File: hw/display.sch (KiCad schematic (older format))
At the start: 1 part

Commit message: revision 2 pcb ordered from itead
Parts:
- removed U?: LPC1785FBD208_551QFP50, usevolt:usevolt-QFP208, symbol LPC1785FBD208_551QFP50
- added BT1: BATTERY_HOLDER_CH7410-2032LFSMD, usevolt:usevolt-BATTERY_HOLDER_CH7410-2032LF, symbol BATTERY_HOLDER_CH7410-2032LFSMD
- added C1, C2, C3, C32, C4, C5, C6, C7, C8: 100nF, kemet:Kemet-CAPC1608X85N, symbol 100nF
- added C22, C29: 12pF, kemet:Kemet-CAPC1608X85N, symbol 12pF
- added J1: AMPSEAL_14_POS_776261-1_V, usevolt:usevolt-AMPSEAL_14_POS_776261-1, symbol AMPSEAL_14_POS_776261-1_V
- added J4: HEADER_MOLEX_52207-0433, usevolt:HEADER_MOLEX_52207-0433, symbol HEADER_MOLEX_52207-0433
- added J5: HEADER_MOLEX_54104-4031, usevolt:HEADER_MOLEX_54104-4031, symbol HEADER_MOLEX_54104-4031
- added R1: 10K, multicomp:Multicomp-RESC1608X60N, symbol 10K
- added U1: MCP2551_SOIC8, usevolt:usevolt-SOIC8, symbol MCP2551_SOIC8
- added U2: ALLIANCE_AS4C4M16SA_TSOP_II, usevolt:usevolt-TSOP_II_54_PIN, symbol ALLIANCE_AS4C4M16SA_TSOP_II
- added U3: WINDBOND_W25Q32FV_SOIC8_W, usevolt:usevolt-SOIC8_W, symbol WINDBOND_W25Q32FV_SOIC8_W
- added U5, U6: MOSFET-N_2N7002W, usevolt:usevolt-SOT323, symbol MOSFET-N_2N7002W
- added X2: XTAL_ABS25-32.768KHZ-T, usevolt:usevolt-XTAL_32.768KHZ-T, symbol XTAL_ABS25-32.768KHZ-T
- added X3: BUZZER_PKM13EPYH4002-B0, usevolt:BUZZER_PKM13EPYH4002-B0, symbol BUZZER_PKM13EPYH4002-B0
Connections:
- net labels added: +3V3, +5V, A0, A1, A10, A11, A2, A3, A4, A5, A6, A7, A8, A9, BA0, BA1, BACKLIGHT, BCKL+, BCKL-, CANH, CANL, DCLK, DE, DQ0, DQ1, DQ10, DQ11, DQ12, DQ13, DQ14, DQ15, DQ2, DQ3, DQ4, DQ5, DQ6, DQ7, DQ8, DQ9, GND, HSYNC, PWR, VD0, VD1, VD10, VD11, VD12, VD13, VD14, VD15, VD16, VD17, VD18, VD19, VD2, VD20, VD21, VD22, VD23, VD3, VD4, VD5, VD6, VD7, VD8, VD9, VDD, VSYNC
- wire segments 0 -> 282
- no-connect marks 0 -> 11

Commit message: PCB was too big for itead, reduced size and ordered one
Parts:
- U1: footprint usevolt:usevolt-SOIC8 -> usevolt:SOIC8
- U2: footprint usevolt:usevolt-TSOP_II_54_PIN -> usevolt:TSOP_II_54_PIN
- U3: footprint usevolt:usevolt-SOIC8_W -> usevolt:SOIC8_W
- U5, U6: footprint usevolt:usevolt-SOT323 -> usevolt:SOT323
- X2: footprint usevolt:usevolt-XTAL_32.768KHZ-T -> usevolt:XTAL_32.768KHZ-T
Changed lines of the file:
@@
 F 0 "U1" H 3250 2846 45  0000 C CNN
 F 1 "MCP2551_SOIC8" H 3250 2930 45  0000 C CNN
-F 2 "usevolt:usevolt-SOIC8" H 2930 3450 20  0001 C CNN
+F 2 "usevolt:SOIC8" H 2930 3450 20  0001 C CNN
 F 3 "http://www.microchip.com/mymicrochip/filehandler.aspx?ddocname=en011797" H 2900 3520 60  0001 C CNN
 F 4 "9758569" H 3500 4120 60  0001 C CNN "2nd Source Part Number"
@@
 F 0 "U3" H 11300 3654 45  0000 C CNN
 F 1 "WINDBOND_W25Q32FV_SOIC8_W" H 11300 3570 45  0000 C CNN
-F 2 "usevolt:usevolt-SOIC8_W" H 11230 3450 20  0001 C CNN
+F 2 "usevolt:SOIC8_W" H 11230 3450 20  0001 C CNN
 F 3 "http://www.winbond.com/resource-files/w25q32fv%20revi%2010202015.pdf" H 10800 3520 60  0001 C CNN
 F 4 "Digi-Key" H 11100 3820 60  0001 C CNN "1st Source"
@@
 F 0 "U2" H 5300 5454 45  0000 C CNN
 F 1 "ALLIANCE_AS4C4M16SA_TSOP_II" H 5300 5370 45  0000 C CNN
-F 2 "usevolt:usevolt-TSOP_II_54_PIN" H 5430 4250 20  0001 C CNN
+F 2 "usevolt:TSOP_II_54_PIN" H 5430 4250 20  0001 C CNN
 F 3 "http://www.alliancememory.com/pdf/dram/64M-AS4C4M16SA-Automotive_v3.0_March%202015.pdf" H 4710 5330 60  0001 C CNN
 F 4 "1450-1258-ND" H 5110 5730 60  0001 C CNN "1st Source Part Number"
@@
 $Bitmap
 Pos 15800 10400
-Scale 1,000000
+Scale 1.000000
 Data
 89 50 4E 47 0D 0A 1A 0A 00 00 00 0D 49 48 44 52 00 00 00 7B 00 00 00 49 08 02 00 00 00 92 17 CE
@@
 F 0 "X2" V 7208 7698 45  0000 L CNN
 F 1 "XTAL_ABS25-32.768KHZ-T" V 7292 7698 45  0000 L CNN
-F 2 "usevolt:usevolt-XTAL_32.768KHZ-T" H 7330 7750 20  0001 C CNN
+F 2 "usevolt:XTAL_32.768KHZ-T" H 7330 7750 20  0001 C CNN
 F 3 "http://www.abracon.com/Resonators/abs25.pdf" H 7320 7620 60  0001 C CNN
 F 4 "1611824" H 7920 8220 60  0001 C CNN "2nd Source Part Number"
@@
 F 0 "U5" H 10400 7844 60  0000 C CNN
 F 1 "MOSFET-N_2N7002W" H 10400 7738 60  0000 C CNN
-F 2 "usevolt:usevolt-SOT323" H 10700 8900 60  0001 C CNN
+F 2 "usevolt:SOT323" H 10700 8900 60  0001 C CNN
 F 3 "http://www.onsemi.com/pub_link/Collateral/2N7002W-D.PDF" H 10550 9000 60  0001 C CNN
 F 4 "2533171" H 10975 8825 60  0001 C CNN "2nd Source Part Number"
@@
 F 0 "U6" H 13200 3350 60  0000 C CNN
 F 1 "MOSFET-N_2N7002W" H 13350 3450 60  0000 C CNN
-F 2 "usevolt:usevolt-SOT323" H 13500 4450 60  0001 C CNN
+F 2 "usevolt:SOT323" H 13500 4450 60  0001 C CNN
 F 3 "http://www.onsemi.com/pub_link/Collateral/2N7002W-D.PDF" H 13350 4550 60  0001 C CNN
 F 4 "2533171" H 13775 4375 60  0001 C CNN "2nd Source Part Number"

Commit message: windows and texts working in UI
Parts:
- U5, U6: symbol MOSFET-N_2N7002W -> MOSFET-N_2N7002W-RESCUE-display
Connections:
- wire segments 282 -> 308

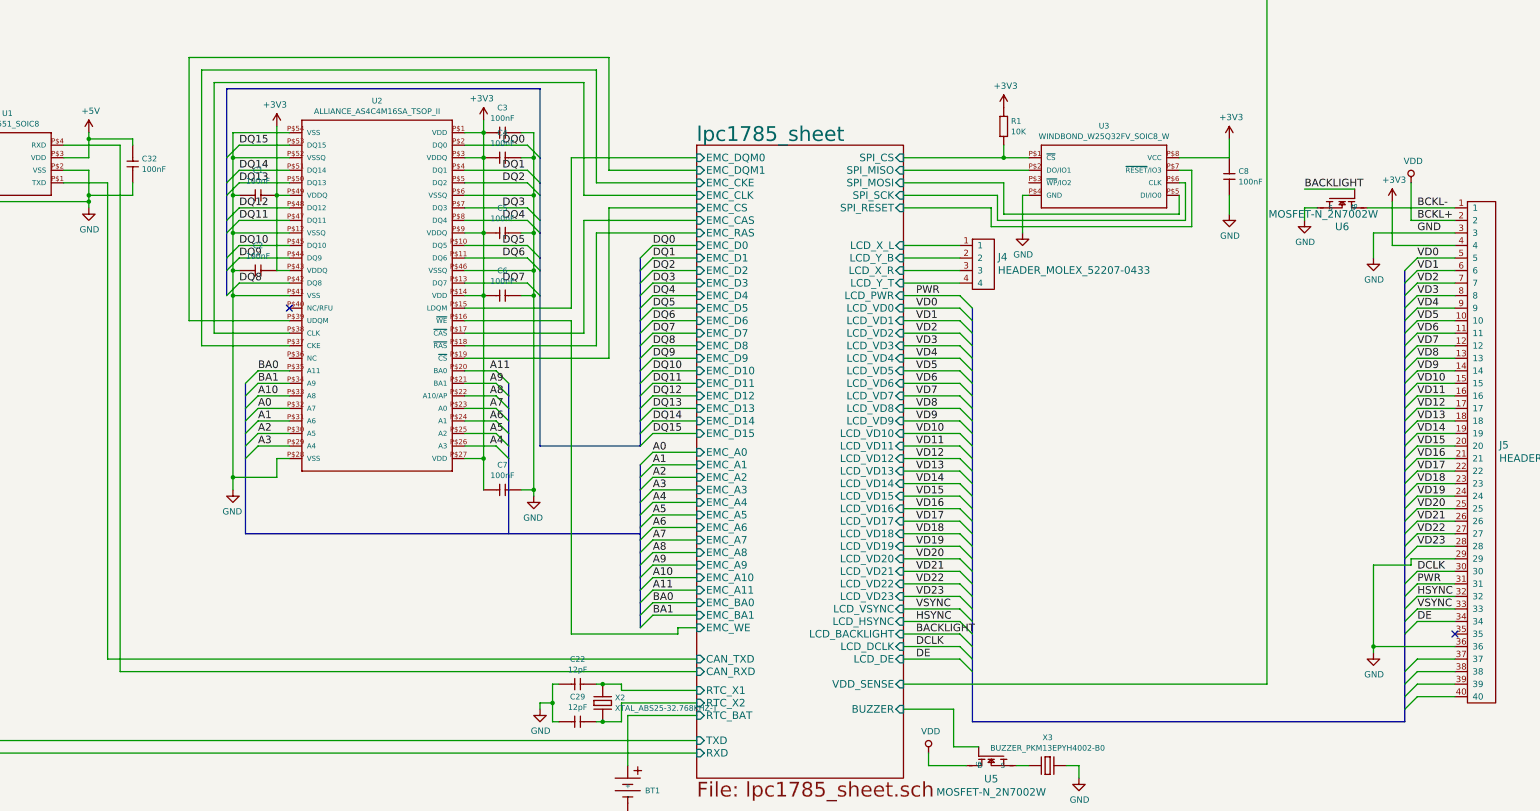
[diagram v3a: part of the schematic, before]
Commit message: Changed LCD interface from RGB888 to RGB565
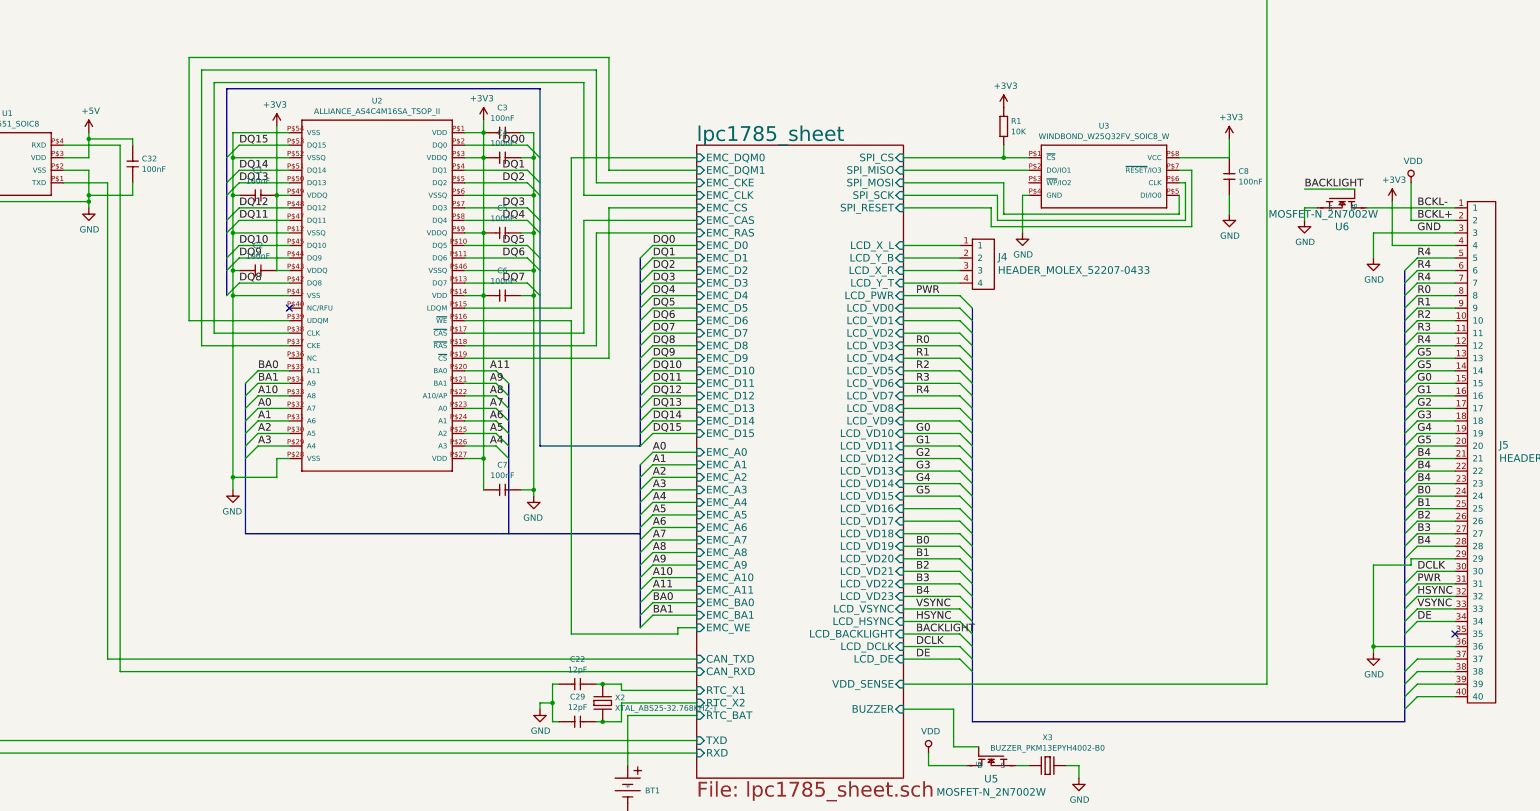
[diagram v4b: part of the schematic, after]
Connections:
- net VD1 is gone; now on net R4: J5.6
- net VD17 is gone; now on net B4: J5.22
- net VD18 is gone; now on net B4: J5.23
- net VD2 is gone; now on net R4: J5.7
- net VD23 is gone; now on net B4: J5.28
- net VD7 is gone; now on net R4: J5.12
- net VD8 is gone; now on net G5: J5.13
- net VD9 is gone; now on net G5: J5.14
- net VD0 renamed R4
- net VD10 renamed G0
- net VD11 renamed G1
- net VD12 renamed G2
- net VD13 renamed G3
- net VD14 renamed G4
- net VD15 renamed G5
- net VD16 renamed B4
- net VD19 renamed B0
- net VD20 renamed B1
- net VD21 renamed B2
- net VD22 renamed B3
- net VD3 renamed R0
- net VD4 renamed R1
- net VD5 renamed R2
- net VD6 renamed R3

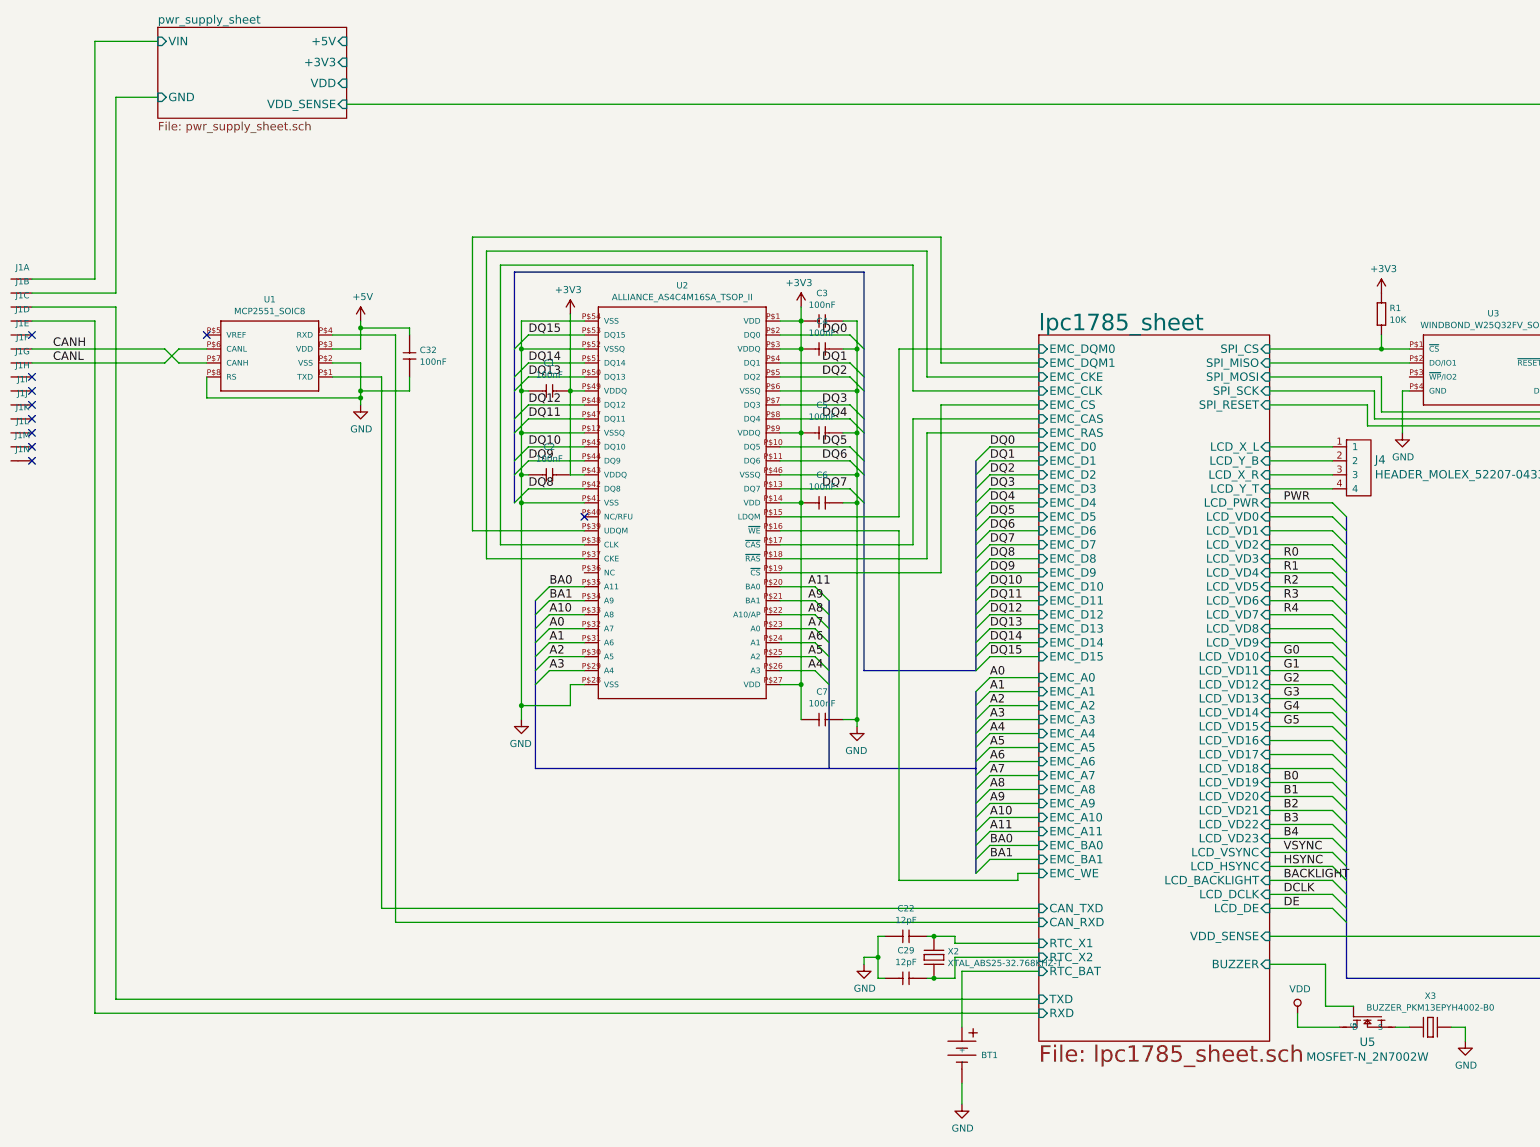
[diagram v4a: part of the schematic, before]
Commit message: HW revision 3 ordered from itead
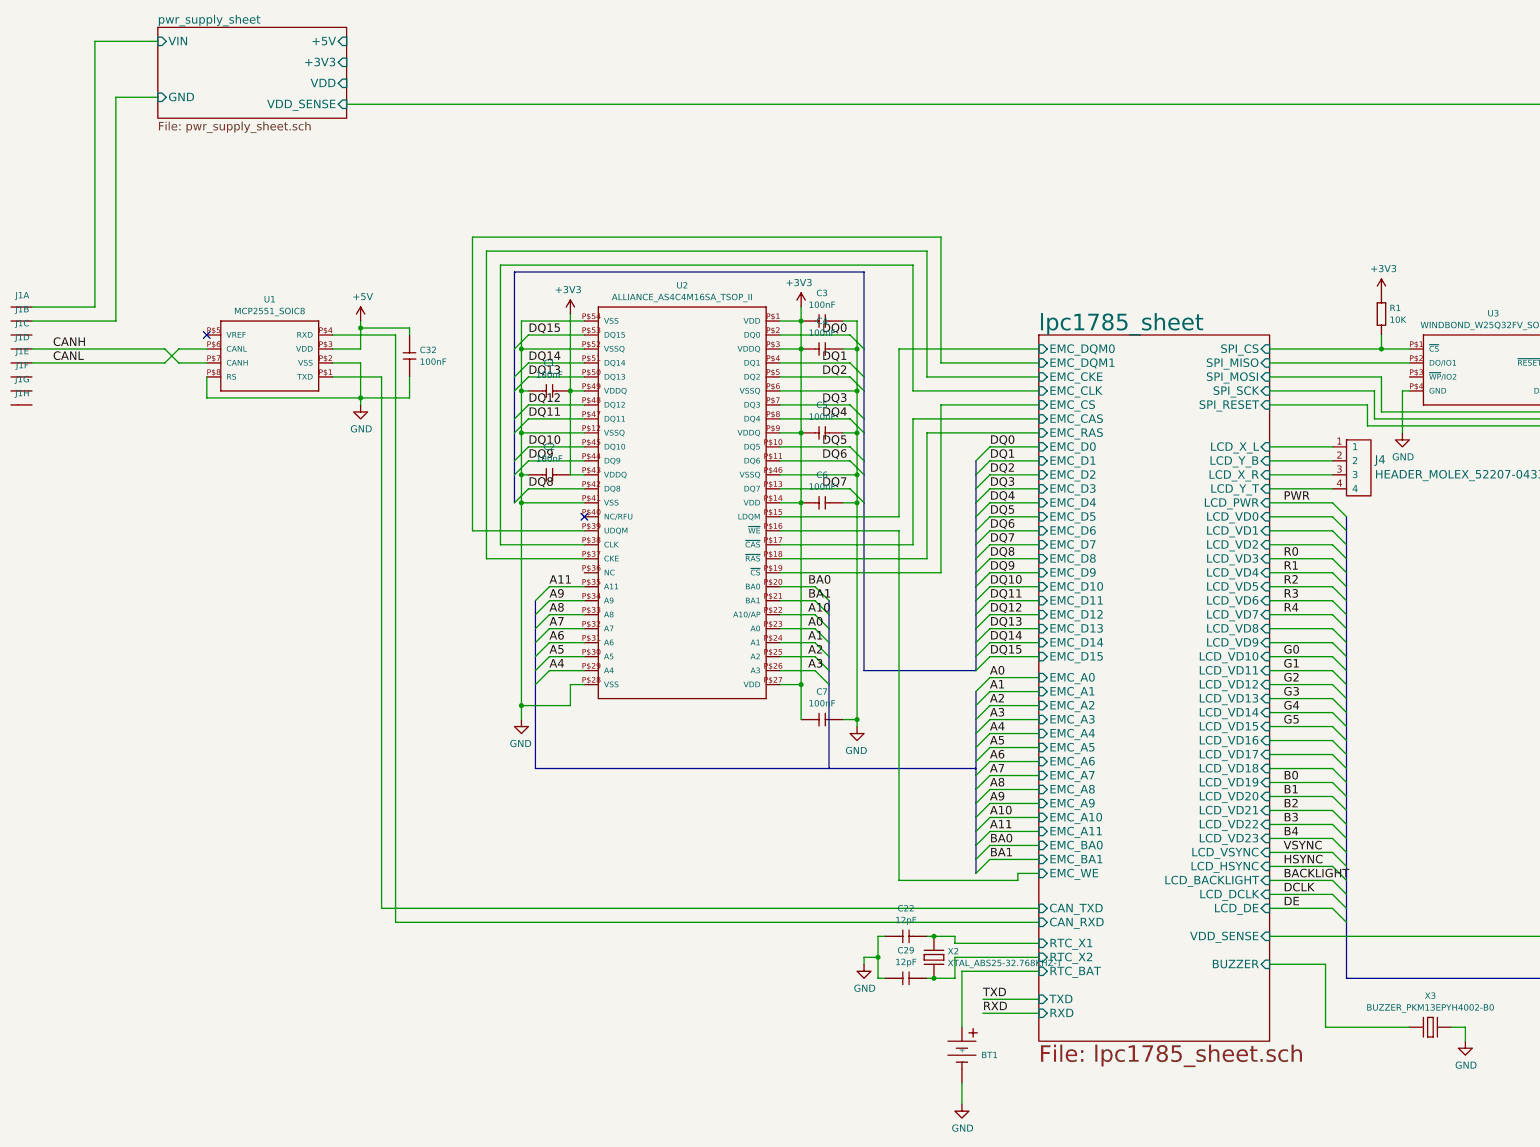
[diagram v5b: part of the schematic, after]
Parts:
- removed J1: AMPSEAL_14_POS_776261-1_V, usevolt:usevolt-AMPSEAL_14_POS_776261-1, symbol AMPSEAL_14_POS_776261-1_V
- removed U5: MOSFET-N_2N7002W, usevolt:SOT323, symbol MOSFET-N_2N7002W-RESCUE-display
- added J1: AMPSEAL_8_POS_776275-1, usevolt:AMPSEAL_8_POS_776275-1, symbol AMPSEAL_8_POS_776275-1
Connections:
- net A0: now also U2.P$23 (A0); no longer U2.P$32 (A7)
- net A1: now also U2.P$24 (A1); no longer U2.P$31 (A6)
- net A10: now also U2.P$22 (A10/AP); no longer U2.P$33 (A8)
- net A11: now also U2.P$35 (A11); no longer U2.P$20 (BA0)
- net A2: now also U2.P$25 (A2); no longer U2.P$30 (A5)
- net A3: now also U2.P$26 (A3); no longer U2.P$29 (A4)
- net A4: now also U2.P$29 (A4); no longer U2.P$26 (A3)
- net A5: now also U2.P$30 (A5); no longer U2.P$25 (A2)
- net A6: now also U2.P$31 (A6); no longer U2.P$24 (A1)
- net A7: now also U2.P$32 (A7); no longer U2.P$23 (A0)
- net A8: now also U2.P$33 (A8); no longer U2.P$22 (A10/AP)
- net A9: now also U2.P$34 (A9); no longer U2.P$21 (BA1)
- net BA0: now also U2.P$20 (BA0); no longer U2.P$35 (A11)
- net BA1: now also U2.P$21 (BA1); no longer U2.P$34 (A9)
- net CANH: now also J1.P$4 (S)
- net CANL: now also J1.P$5 (S)
- net lpc1785_sheet/BUZZER: now also X3.1 (P$1)
- net pwr_supply_sheet/GND: now also J1.P$2 (S)
- net pwr_supply_sheet/VIN: now also J1.P$1 (S)
- no-connect marks 11 -> 3
